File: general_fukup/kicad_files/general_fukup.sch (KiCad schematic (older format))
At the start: 26 parts, among them J1 INPUT, J2 OUTPUT, Q1 BC337, Q2 BC337, Q3 BC327, SW1 SW_Rotary2x6

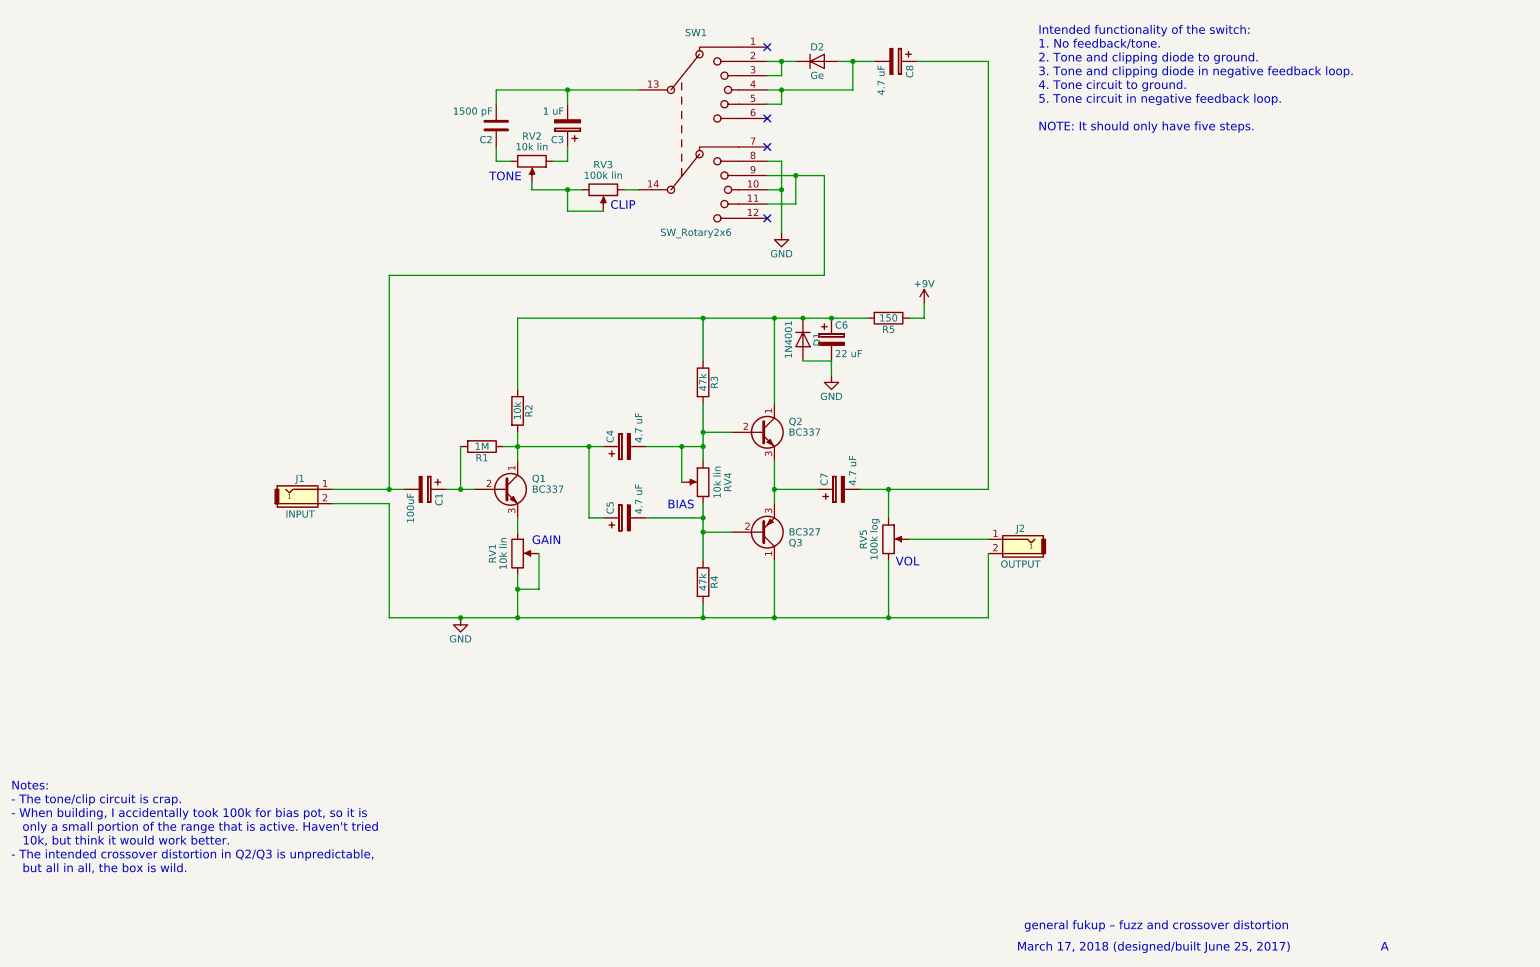
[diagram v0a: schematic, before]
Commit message: Add PCB layout for General Fukup
Not tested, not pretty, it is my first attempt ever. So there.
The tone control is not included, partly because it's crappy,
but mainly because in the box, it is very crowded.
Also, its pots cannot be mounted on this PCB anyway (unless
it is a very wide box.
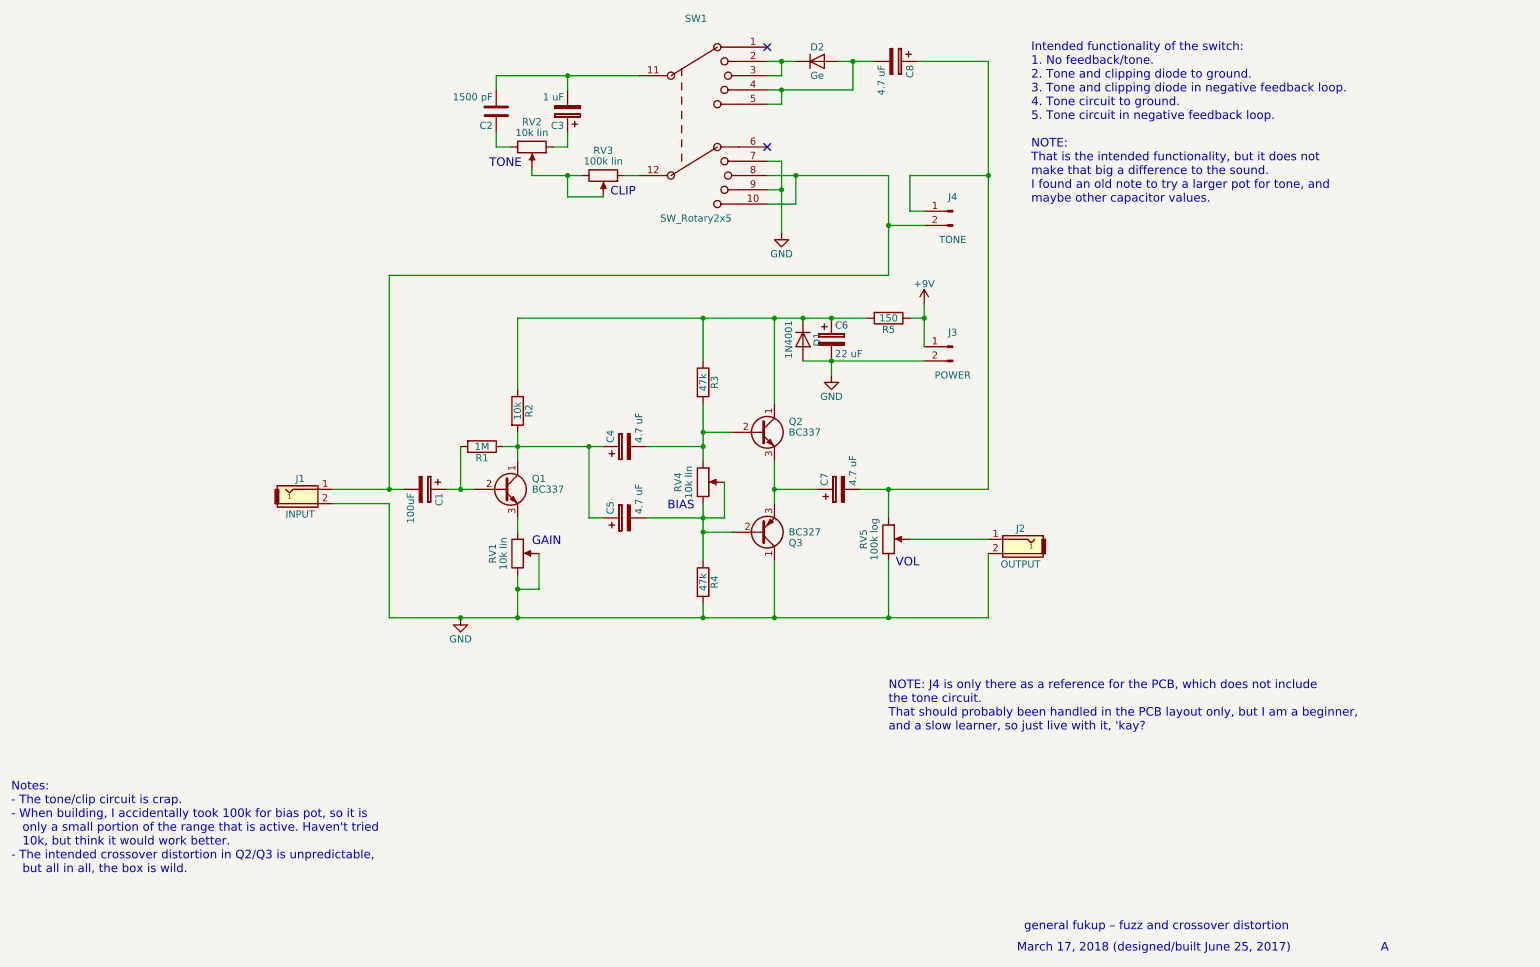
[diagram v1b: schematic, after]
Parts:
- removed SW1: SW_Rotary2x6, symbol SW_Rotary2x6
- added J3: POWER, Pin_Headers:Pin_Header_Straight_1x02_Pitch2.54mm, symbol Conn_01x02_Male
- added J4: TONE, Pin_Headers:Pin_Header_Straight_1x02_Pitch2.54mm, symbol Conn_01x02_Male
- added SW1: SW_Rotary2x5, Pin_Headers:Pin_Header_Straight_2x06_Pitch2.54mm, symbol SW_Rotary2x5
- C1, C3, C4, C5, C6, C7, C8: footprint (none) -> Capacitors_THT:CP_Radial_D5.0mm_P2.50mm
- C2: footprint (none) -> Capacitors_THT:C_Disc_D10.5mm_W5.0mm_P5.00mm
- D1: footprint (none) -> Diodes_THT:D_DO-41_SOD81_P5.08mm_Vertical_AnodeUp
- D2: footprint (none) -> Diodes_THT:D_DO-15_P10.16mm_Horizontal
- J1, J2: footprint (none) -> Pin_Headers:Pin_Header_Straight_1x02_Pitch2.54mm
- R1, R2, R3, R4, R5: footprint (none) -> Resistors_THT:R_Axial_DIN0207_L6.3mm_D2.5mm_P10.16mm_Horizontal
- RV1, RV2, RV3, RV4: footprint (none) -> Potentiometers:Potentiometer_WirePads
- RV5: footprint (none) -> Pin_Headers:Pin_Header_Straight_1x03_Pitch2.54mm
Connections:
- net +9V: now also J3.1 (Pin_1)
- net GND: now also J3.2 (Pin_2), SW1.7, SW1.9
- net at C4.2, Q2.2 (B), R3.2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: no longer RV4.2
- net at C5.2, Q3.2 (B), R4.1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: now also RV4.2
- net at RV3.1: now also SW1.12
- net at C7.2, C8.1, RV5.1: now also J4.1 (Pin_1)
- net at C1.2, J1.1: now also J4.2 (Pin_2), SW1.10, SW1.8
- net at C2.2, C3.2: now also SW1.11
- net at D2.1 (K): now also SW1.2, SW1.3
- net at C8.2, D2.2 (A): now also SW1.4, SW1.5
- no-connect marks 4 -> 2
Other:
- note added: "Intended functionality of the switch:\n1. No feedback/tone.\n2. Tone and clipping diode to ground. \n3. Tone and clipping diode in negative feedback loop.\n4. Tone circuit to ground. \n5. Tone circuit in negative feedback loop.\n\nNOTE: \nThat is the intended functionality, but it does not\nmake that big a difference to the sound.\nI found an old note to try a larger pot for tone, and\nmaybe othe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"
- note added: "NOTE: J4 is only there as a reference for the PCB, which does not include \nthe tone circuit. \nThat should probably been handled in the PCB layout only, but I am a beginner,\nand a slow learner, so just live with it, 'kay?"
- note removed: "Intended functionality of the switch:\n1. No feedback/tone.\n2. Tone and clipping diode to ground. \n3. Tone and clipping diode in negative feedback loop.\n4. Tone circuit to ground. \n5. Tone circuit in negative feedback loop.\n\nNOTE: It should only have five steps."
- moved on the sheet: C2, C3, RV2, RV3
